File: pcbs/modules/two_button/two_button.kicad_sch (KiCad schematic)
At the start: 5 parts, among them SW1 SW_Push, SW2 SW_Push

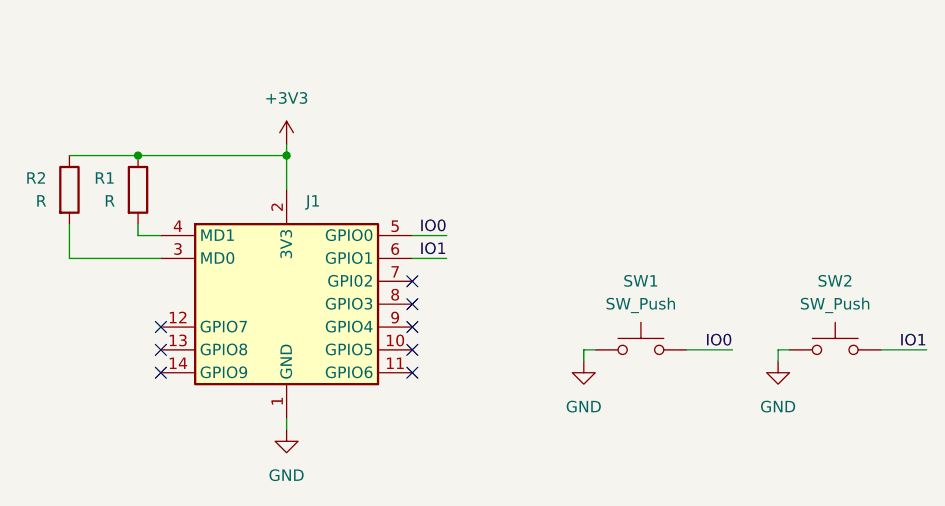
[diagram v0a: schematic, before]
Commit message: added mounting holes to two button module
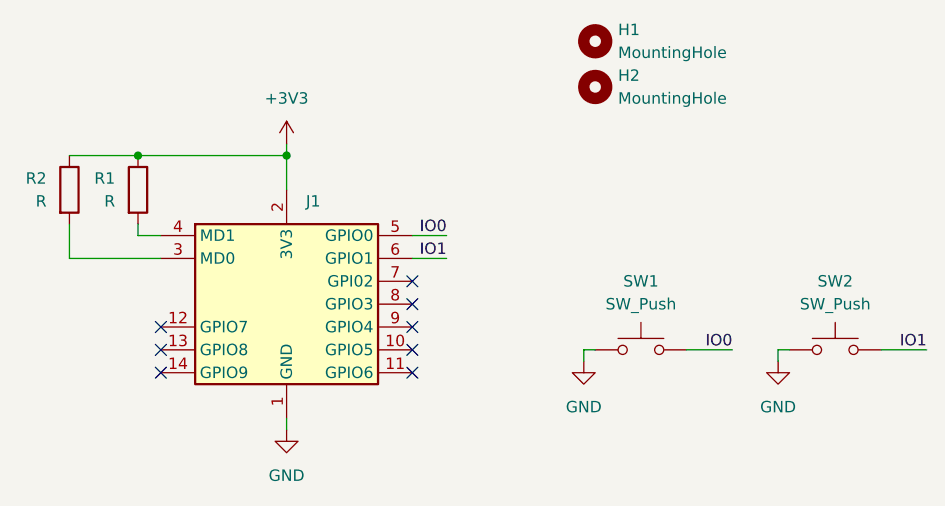
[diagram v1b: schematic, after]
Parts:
- added H1, H2: MountingHole, MountingHole:MountingHole_2.2mm_M2, symbol Mechanical:MountingHole
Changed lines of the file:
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@@
+	)
+	(symbol
+		(lib_id "Mechanical:MountingHole")
+		(at 120.65 63.5 0)
+		(unit 1)
+		(body_style 1)
+		(exclude_from_sim no)
+		(in_bom no)
+		(on_board yes)
+		(in_pos_files yes)
+		(dnp no)
+		(fields_autoplaced yes)
+		(property "Reference" "H1"
+			(at 123.19 62.2299 0)
+			(show_name no)
+			(do_not_autoplace no)
+			(effects
+				(font
+					(size 1.27 1.27)
+				)
+				(justify left)
+			)
+		)
+		(property "Value" "MountingHole"
+			(at 123.19 64.7699 0)
+			(show_name no)
+			(do_not_autoplace no)
+			(effects
+				(font
+					(size 1.27 1.27)
+				)
+				(justify left)
+			)
+		)
+		(property "Footprint" "MountingHole:MountingHole_2.2mm_M2"
+			(at 120.65 63.5 0)
+			(hide yes)
+			(show_name no)
+			(do_not_autoplace no)
+			(effects
+				(font
+					(size 1.27 1.27)
+				)
+			)
+		)
+		(property "Datasheet" ""
+			(at 120.65 63.5 0)
+			(hide yes)
+			(show_name no)
+			(do_not_autoplace no)
+			(effects
+				(font
+					(size 1.27 1.27)
+				)
+			)
+		)
+		(property "Description" "Mounting Hole without connection"
+			(at 120.65 63.5 0)
+			(hide yes)
+			(show_name no)
+			(do_not_autoplace no)
+			(effects
+				(font
+					(size 1.27 1.27)
+				)
+			)
+		)
+		(instances
+			(project "two_button"
+				(path "/4f0f379b-9acc-49b4-81dc-86c4ce2d2a86"
+					(reference "H1")
+					(unit 1)
+				)
+			)
+		)
 	)
 	(symbol
@@
 					(unit 1)
 				)
+			)
+		)
+	)
+	(symbol
+		(lib_id "Mechanical:MountingHole")
+		(at 120.65 68.58 0)
+		(unit 1)
+		(body_style 1)
+		(exclude_from_sim no)
+		(in_bom no)
+		(on_board yes)
+		(in_pos_files yes)
+		(dnp no)
+		(fields_autoplaced yes)
+		(property "Reference" "H2"
+			(at 123.19 67.3099 0)
+			(show_name no)
+			(do_not_autoplace no)
+			(effects
+				(font
+					(size 1.27 1.27)
+				)
+				(justify left)
+			)
+		)
+		(property "Value" "MountingHole"
+			(at 123.19 69.8499 0)
+			(show_name no)
+			(do_not_autoplace no)
+			(effects
+				(font
+					(size 1.27 1.27)
+				)
+				(justify left)
+			)
+		)
+		(property "Footprint" "MountingHole:MountingHole_2.2mm_M2"
+			(at 120.65 68.58 0)
+			(hide yes)
+			(show_name no)
+			(do_not_autoplace no)
+			(effects
+				(font
+					(size 1.27 1.27)
+				)
+			)
+		)
+		(property "Datasheet" ""
+			(at 120.65 68.58 0)
+			(hide yes)
+			(show_name no)
+			(do_not_autoplace no)
+			(effects
+				(font
+					(size 1.27 1.27)
+				)
+			)
+		)
+		(property "Description" "Mounting Hole without connection"
+			(at 120.65 68.58 0)
+			(hide yes)
+			(show_name no)
+			(do_not_autoplace no)
+			(effects
+				(font
+					(size 1.27 1.27)
+				)
+			)
+		)
+		(instances
+			(project "two_button"
+				(path "/4f0f379b-9acc-49b4-81dc-86c4ce2d2a86"
+					(reference "H2")
+					(unit 1)
+				)
